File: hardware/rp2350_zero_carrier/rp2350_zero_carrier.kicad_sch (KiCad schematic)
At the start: 8 parts, among them J1 RP2350-Zero_Header(20pin,plac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, J2 USB-A_Host(Neltron_5075AR-04-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, SW1 1回路2接点スイッチ(3pin,NKK_115643,ON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, SW2 1回路2接点スイッチ(3pin,NKK_115643,ON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, SW3 1回路2接点スイッチ(3pin,NKK_115643,ON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

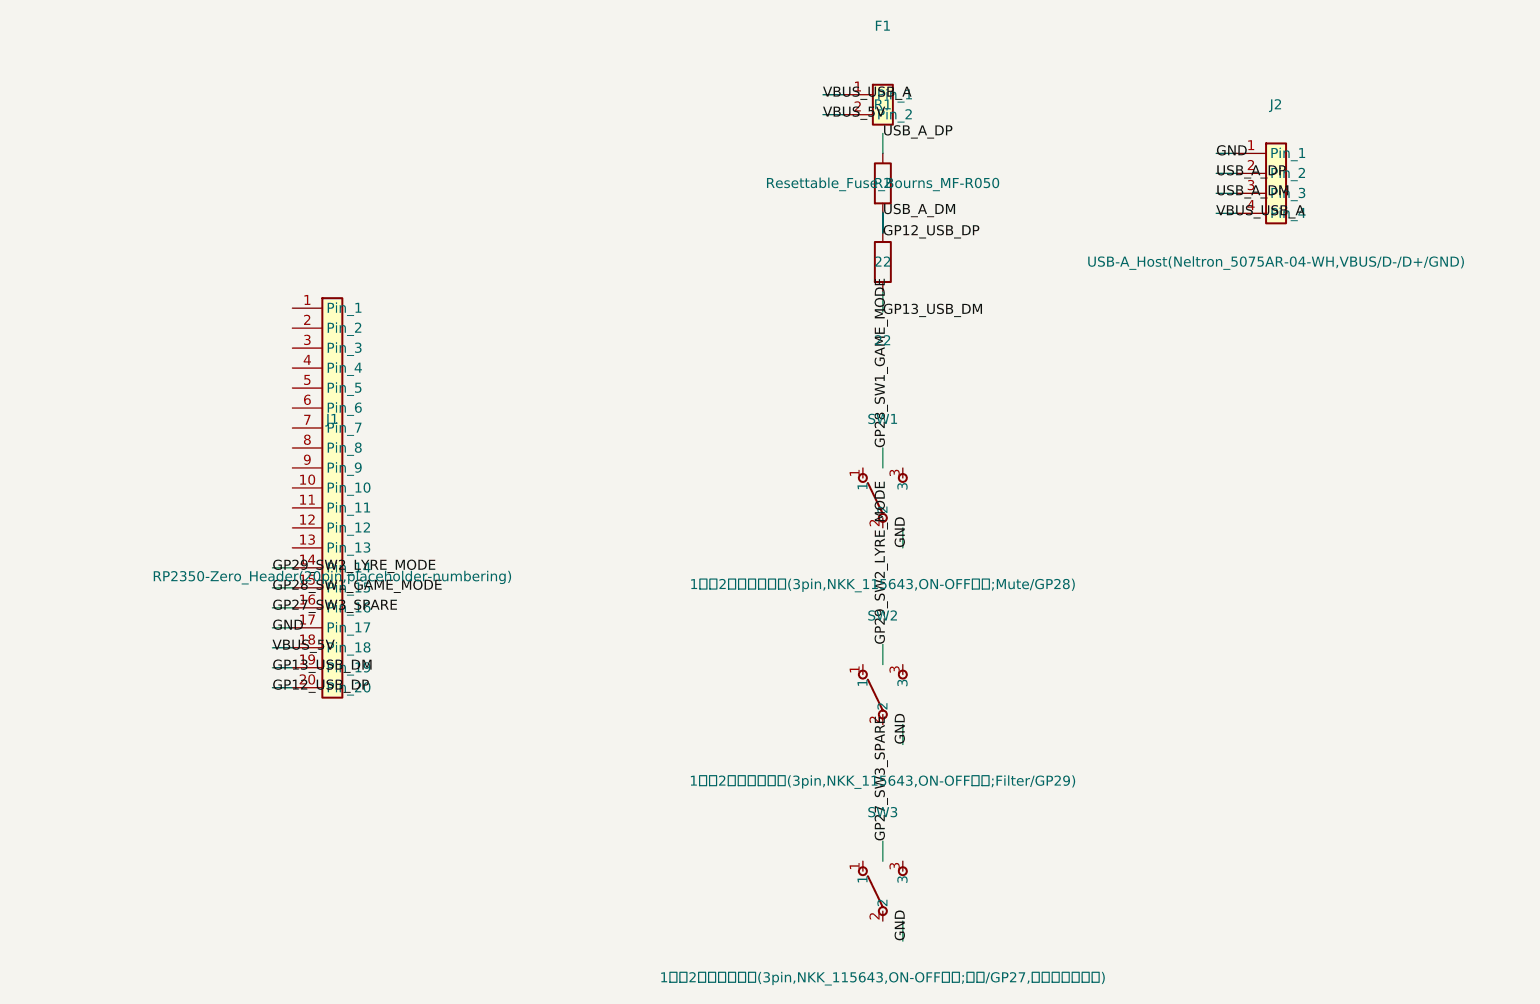
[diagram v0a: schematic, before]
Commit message: USB Host D+/D-をGP12/GP13からGP14/GP15へ訂正
実機のRP2350-Zeroピンヘッダー配置表により、GP12/GP13は20pinヘッダーに
物理的に存在しない(はんだ付け専用パッドのみ)と判明したため訂正。
唯一2本だけの独立列で隣接ペア要件も満たすGP14(D+)/GP15(D-)に変更。
J1のプレースホルダーpin番号を1/2→10/11(表内の実ピン番号に対応)へ、
GP27/28/29用も5/6/7→13/14/15へ付け替え。R1/R2は結線ラベルの変更のみ
(定数変更なし)。

ファームウェア側の対応(PIN_USB_HOST_DP を 12→14 に変更)は別タスク。

Co-Authored-By: Claude Sonnet 5 <noreply@anthropic.com>
Claude-Session: https://claude.ai/code/session_01E7QH5gCzZj3tVha83XRuUt
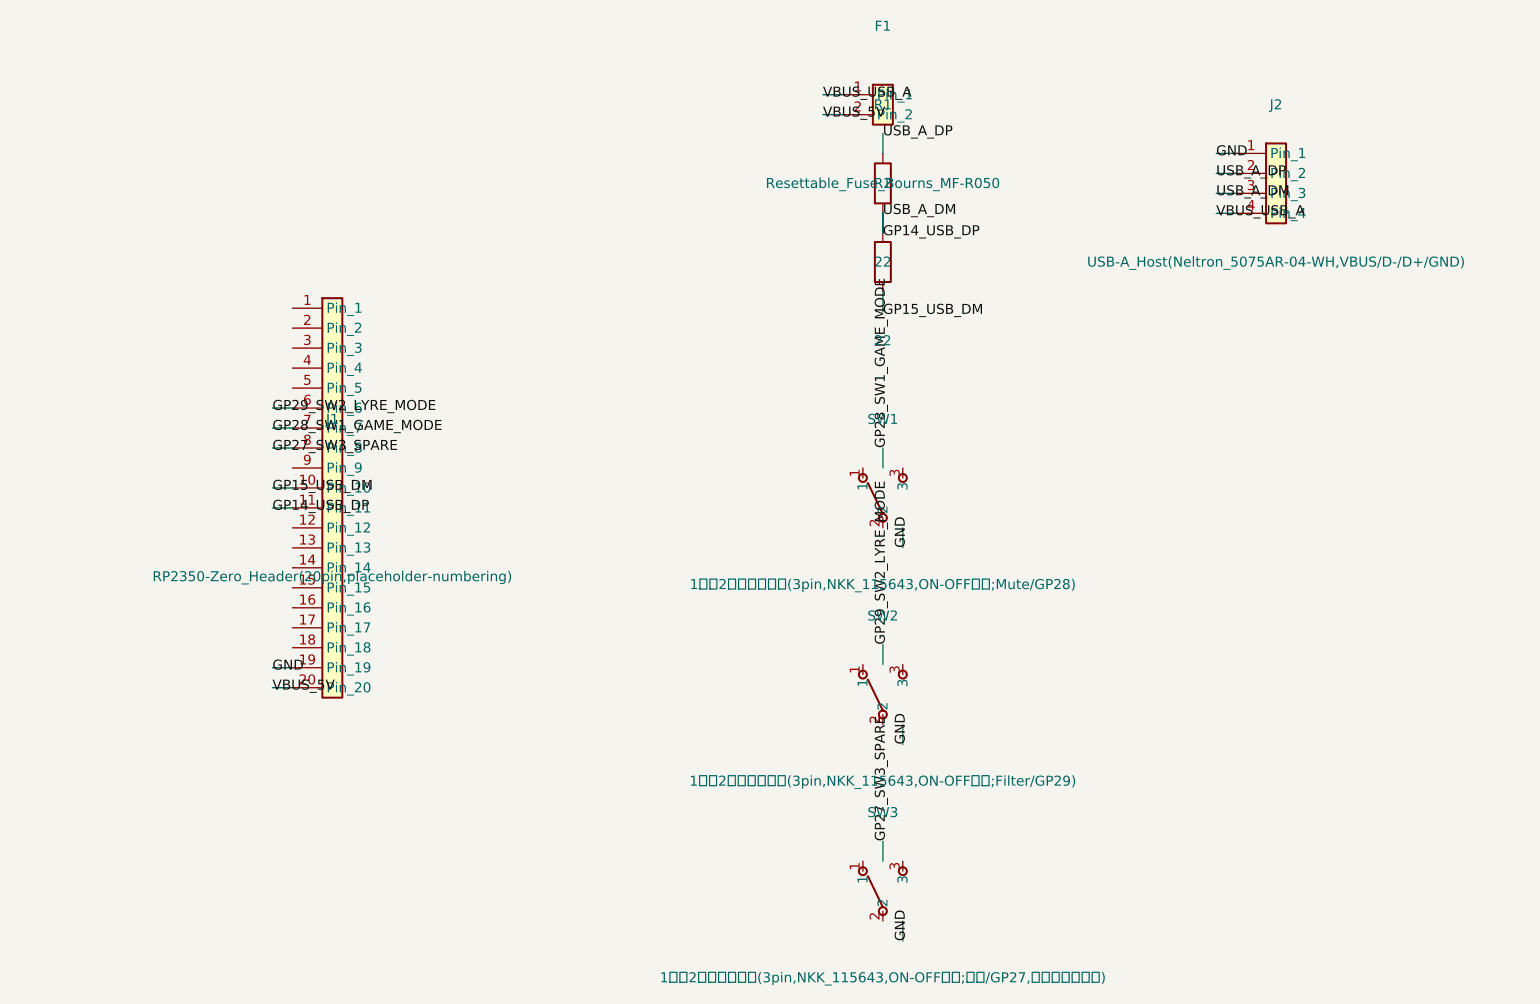
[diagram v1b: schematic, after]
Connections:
- net GND: now also J1.19 (Pin_19); no longer J1.17 (Pin_17)
- net GP27_SW3_SPARE: now also J1.8 (Pin_8); no longer J1.16 (Pin_16)
- net GP28_SW1_GAME_MODE: now also J1.7 (Pin_7); no longer J1.15 (Pin_15)
- net GP29_SW2_LYRE_MODE: now also J1.6 (Pin_6); no longer J1.14 (Pin_14)
- net VBUS_5V: now also J1.20 (Pin_20); no longer J1.18 (Pin_18)
- net GP15_USB_DM: now reaches J1.10 (Pin_10)
- net GP15_USB_DM: now also R2.2
- net GP14_USB_DP: now reaches J1.11 (Pin_11)
- net GP14_USB_DP: now also J2.3 (Pin_3), R1.2, R2.1
- removed net GP12_USB_DP: J1.20 (Pin_20), J2.3 (Pin_3), R1.2, R2.1
- removed net GP13_USB_DM: J1.19 (Pin_19), R2.2
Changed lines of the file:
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@@
   (wire (pts (xy 34.92 154.13) (xy 32.38 154.13)) (stroke (width 0) (type default)))
   (wire (pts (xy 34.92 151.59) (xy 32.38 151.59)) (stroke (width 0) (type default)))
-  (wire (pts (xy 34.92 149.05) (xy 32.38 149.05)) (stroke (width 0) (type default)))
-  (wire (pts (xy 34.92 146.51) (xy 32.38 146.51)) (stroke (width 0) (type default)))
-  (wire (pts (xy 34.92 143.97) (xy 32.38 143.97)) (stroke (width 0) (type default)))
-  (wire (pts (xy 34.92 141.43) (xy 32.38 141.43)) (stroke (width 0) (type default)))
-  (wire (pts (xy 34.92 138.89) (xy 32.38 138.89)) (stroke (width 0) (type default)))
+  (wire (pts (xy 34.92 131.27) (xy 32.38 131.27)) (stroke (width 0) (type default)))
+  (wire (pts (xy 34.92 128.73) (xy 32.38 128.73)) (stroke (width 0) (type default)))
+  (wire (pts (xy 34.92 123.65) (xy 32.38 123.65)) (stroke (width 0) (type default)))
+  (wire (pts (xy 34.92 121.11) (xy 32.38 121.11)) (stroke (width 0) (type default)))
+  (wire (pts (xy 34.92 118.57) (xy 32.38 118.57)) (stroke (width 0) (type default)))
   (wire (pts (xy 110 93.81) (xy 110 96.35)) (stroke (width 0) (type default)))
   (wire (pts (xy 110 86.19) (xy 110 83.65)) (stroke (width 0) (type default)))
@@
   (wire (pts (xy 110 176.19) (xy 110 173.65)) (stroke (width 0) (type default)))
   (wire (pts (xy 112.54 183.81) (xy 112.54 186.35)) (stroke (width 0) (type default)))
-  (label "GP12_USB_DP" (at 32.38 154.13 0) (effects (font (size 1.27 1.27)) (justify left)))
-  (label "GP13_USB_DM" (at 32.38 151.59 0) (effects (font (size 1.27 1.27)) (justify left)))
-  (label "VBUS_5V" (at 32.38 149.05 0) (effects (font (size 1.27 1.27)) (justify left)))
-  (label "GND" (at 32.38 146.51 0) (effects (font (size 1.27 1.27)) (justify left)))
-  (label "GP27_SW3_SPARE" (at 32.38 143.97 0) (effects (font (size 1.27 1.27)) (justify left)))
-  (label "GP28_SW1_GAME_MODE" (at 32.38 141.43 0) (effects (font (size 1.27 1.27)) (justify left)))
-  (label "GP29_SW2_LYRE_MODE" (at 32.38 138.89 0) (effects (font (size 1.27 1.27)) (justify left)))
-  (label "GP12_USB_DP" (at 110 96.35 0) (effects (font (size 1.27 1.27)) (justify left)))
+  (label "VBUS_5V" (at 32.38 154.13 0) (effects (font (size 1.27 1.27)) (justify left)))
+  (label "GND" (at 32.38 151.59 0) (effects (font (size 1.27 1.27)) (justify left)))
+  (label "GP14_USB_DP" (at 32.38 131.27 0) (effects (font (size 1.27 1.27)) (justify left)))
+  (label "GP15_USB_DM" (at 32.38 128.73 0) (effects (font (size 1.27 1.27)) (justify left)))
+  (label "GP27_SW3_SPARE" (at 32.38 123.65 0) (effects (font (size 1.27 1.27)) (justify left)))
+  (label "GP28_SW1_GAME_MODE" (at 32.38 121.11 0) (effects (font (size 1.27 1.27)) (justify left)))
+  (label "GP29_SW2_LYRE_MODE" (at 32.38 118.57 0) (effects (font (size 1.27 1.27)) (justify left)))
+  (label "GP14_USB_DP" (at 110 96.35 0) (effects (font (size 1.27 1.27)) (justify left)))
   (label "USB_A_DP" (at 110 83.65 0) (effects (font (size 1.27 1.27)) (justify left)))
-  (label "GP13_USB_DM" (at 110 106.35 0) (effects (font (size 1.27 1.27)) (justify left)))
+  (label "GP15_USB_DM" (at 110 106.35 0) (effects (font (size 1.27 1.27)) (justify left)))
   (label "USB_A_DM" (at 110 93.65 0) (effects (font (size 1.27 1.27)) (justify left)))
   (label "VBUS_5V" (at 102.38 81.27 0) (effects (font (size 1.27 1.27)) (justify left)))

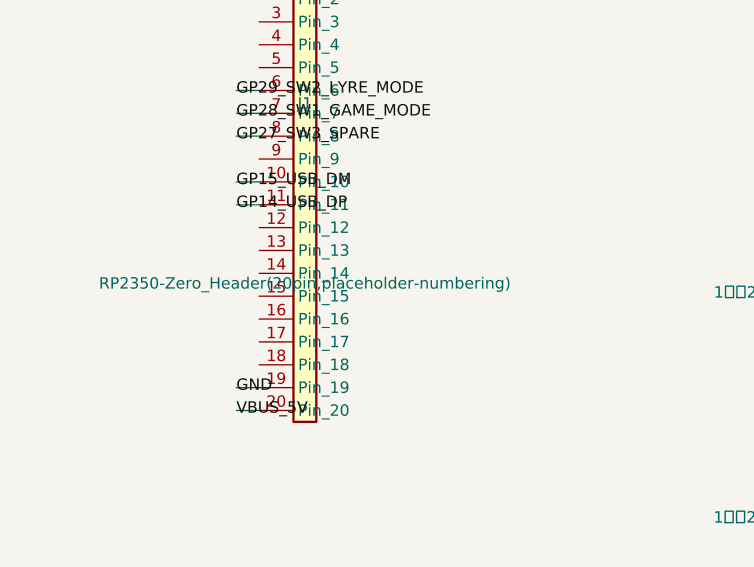
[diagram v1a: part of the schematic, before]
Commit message: J1にユーザー確定のRP2350-Zero実ピン配置footprintを追加
外形18.0x23.5mm・ピッチ2.54mm・列間15.24mm(600mil)・穴径1.0mm/パッド径
1.6mmの実測ピン配置表(2026-08-20確定)に基づくカスタムfootprintを作成。
原点=モジュール中心。pin10/11(GP14/GP15)はUSB D+/D-用の独立2pin列。
標準ライブラリの汎用1x20 footprintから差し替え。

Co-Authored-By: Claude Sonnet 5 <noreply@anthropic.com>
Claude-Session: https://claude.ai/code/session_01E7QH5gCzZj3tVha83XRuUt
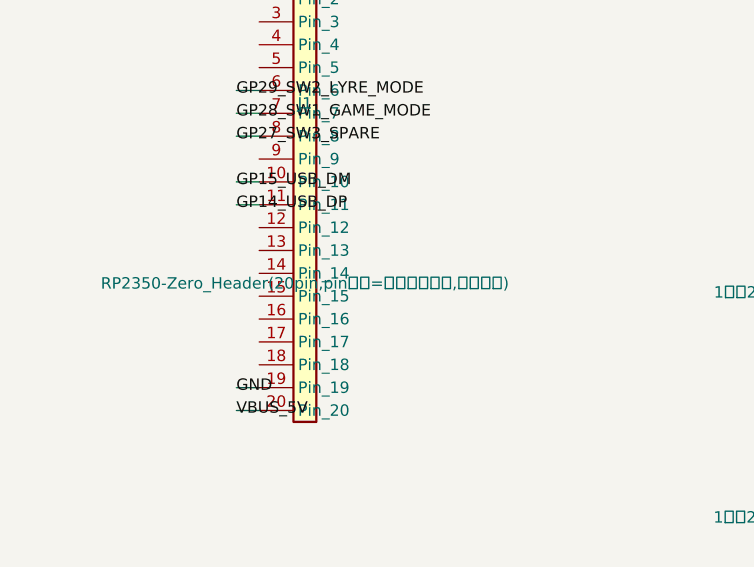
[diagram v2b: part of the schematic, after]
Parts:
- J1: value RP2350-Zero_Header(20pin,placeholder-numbering) -> RP2350-Zero_Header(20pin,pin番号=実物ピン番号,確定済み); footprint Connector_PinSocket_2.54mm:PinSocket_1x20_P2.54mm_Vertical -> rp2350_zero_carrier:RP2350_Zero_Header_20p
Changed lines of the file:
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@@
     (in_bom yes) (on_board yes) (dnp no) (fields_autoplaced yes)
     (property "Reference" "J1" (at 40 120 0) (effects (font (size 1.27 1.27))))
-    (property "Value" "RP2350-Zero_Header(20pin,placeholder-numbering)" (at 40 140 0) (effects (font (size 1.27 1.27))))
-    (property "Footprint" "Connector_PinSocket_2.54mm:PinSocket_1x20_P2.54mm_Vertical" (at 40 130 0) (effects (font (size 1.27 1.27)) hide))
+    (property "Value" "RP2350-Zero_Header(20pin,pin番号=実物ピン番号,確定済み)" (at 40 140 0) (effects (font (size 1.27 1.27))))
+    (property "Footprint" "rp2350_zero_carrier:RP2350_Zero_Header_20p" (at 40 130 0) (effects (font (size 1.27 1.27)) hide))
     (property "Datasheet" "" (at 40 130 0) (effects (font (size 1.27 1.27)) hide))
     (pin "1")

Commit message: R1/R2のfootprintをKiCad標準ライブラリ参照から自作品に差し替え
標準ライブラリ 'Resistor_THT:R_Axial_DIN0207_...' は実際のパッド形状を
この環境で確認する手段がないため、他の自作footprintと同様に丸パッド
(1.6mm/ドリル0.8mm・ピッチ10.16mm)のカスタムfootprintに統一した。
電気的な変更はない。

Co-Authored-By: Claude Sonnet 5 <noreply@anthropic.com>
Claude-Session: https://claude.ai/code/session_01E7QH5gCzZj3tVha83XRuUt
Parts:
- R1, R2: footprint Resistor_THT:R_Axial_DIN0207_L6.3mm_D2.5mm_P10.16mm_Horizontal -> rp2350_zero_carrier:R_Axial_THT_P10.16mm
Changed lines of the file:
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@@
     (property "Reference" "R1" (at 110 80 0) (effects (font (size 1.27 1.27))))
     (property "Value" "22" (at 110 100 0) (effects (font (size 1.27 1.27))))
-    (property "Footprint" "Resistor_THT:R_Axial_DIN0207_L6.3mm_D2.5mm_P10.16mm_Horizontal" (at 110 90 0) (effects (font (size 1.27 1.27)) hide))
+    (property "Footprint" "rp2350_zero_carrier:R_Axial_THT_P10.16mm" (at 110 90 0) (effects (font (size 1.27 1.27)) hide))
     (property "Datasheet" "" (at 110 90 0) (effects (font (size 1.27 1.27)) hide))
     (pin "1")
@@
     (property "Reference" "R2" (at 110 90 0) (effects (font (size 1.27 1.27))))
     (property "Value" "22" (at 110 110 0) (effects (font (size 1.27 1.27))))
-    (property "Footprint" "Resistor_THT:R_Axial_DIN0207_L6.3mm_D2.5mm_P10.16mm_Horizontal" (at 110 100 0) (effects (font (size 1.27 1.27)) hide))
+    (property "Footprint" "rp2350_zero_carrier:R_Axial_THT_P10.16mm" (at 110 100 0) (effects (font (size 1.27 1.27)) hide))
     (property "Datasheet" "" (at 110 100 0) (effects (font (size 1.27 1.27)) hide))
     (pin "1")
